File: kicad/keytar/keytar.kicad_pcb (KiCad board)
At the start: 2 copper layers, 70 x 90 mm, 40 parts, among them J1 , J2 USB_B, J3 AudioJack2, J4 Conn_01x04, J5 USB_A, J6 Mini-DIN-6-Shielded, J7 Conn_01x04, Q1 BSS138, Q2 BSS138, SW1 SW_DPST_x2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

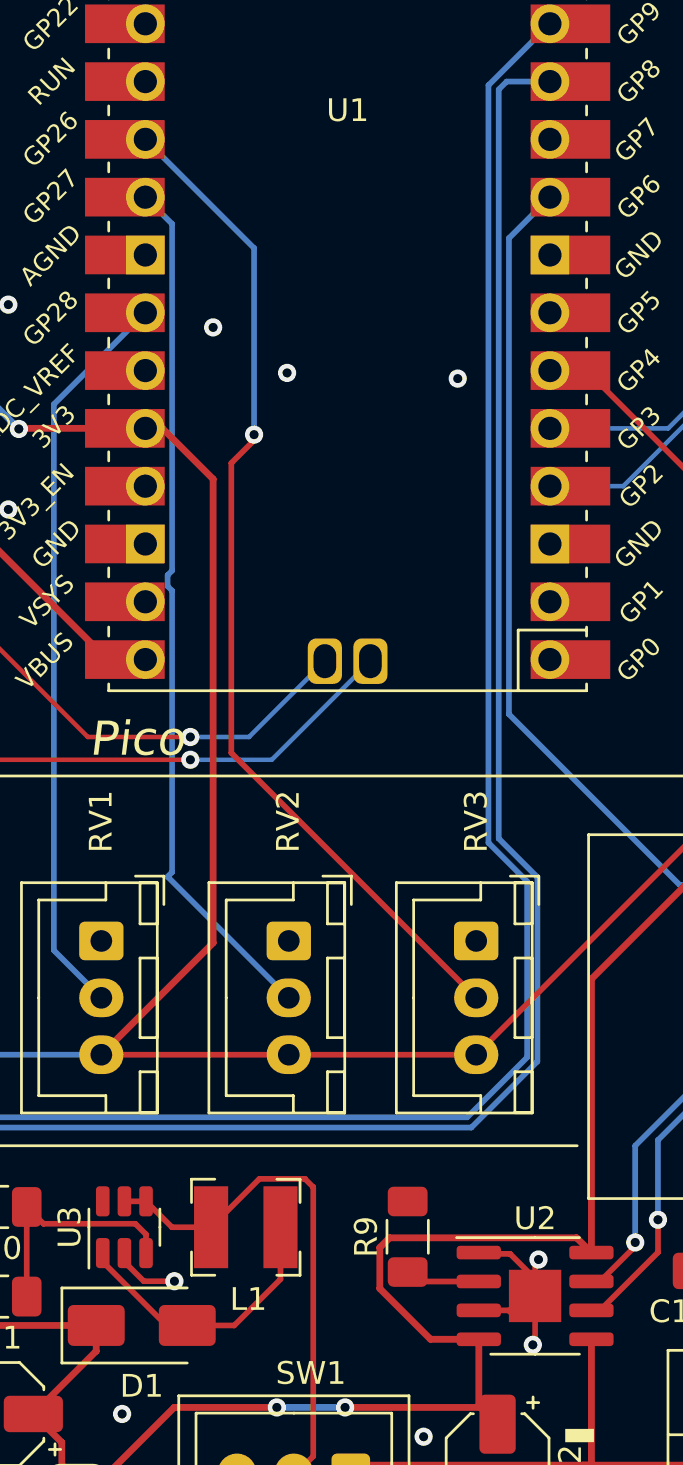
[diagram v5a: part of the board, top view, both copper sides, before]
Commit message: kicad: add voltage divider for battery voltage measurement
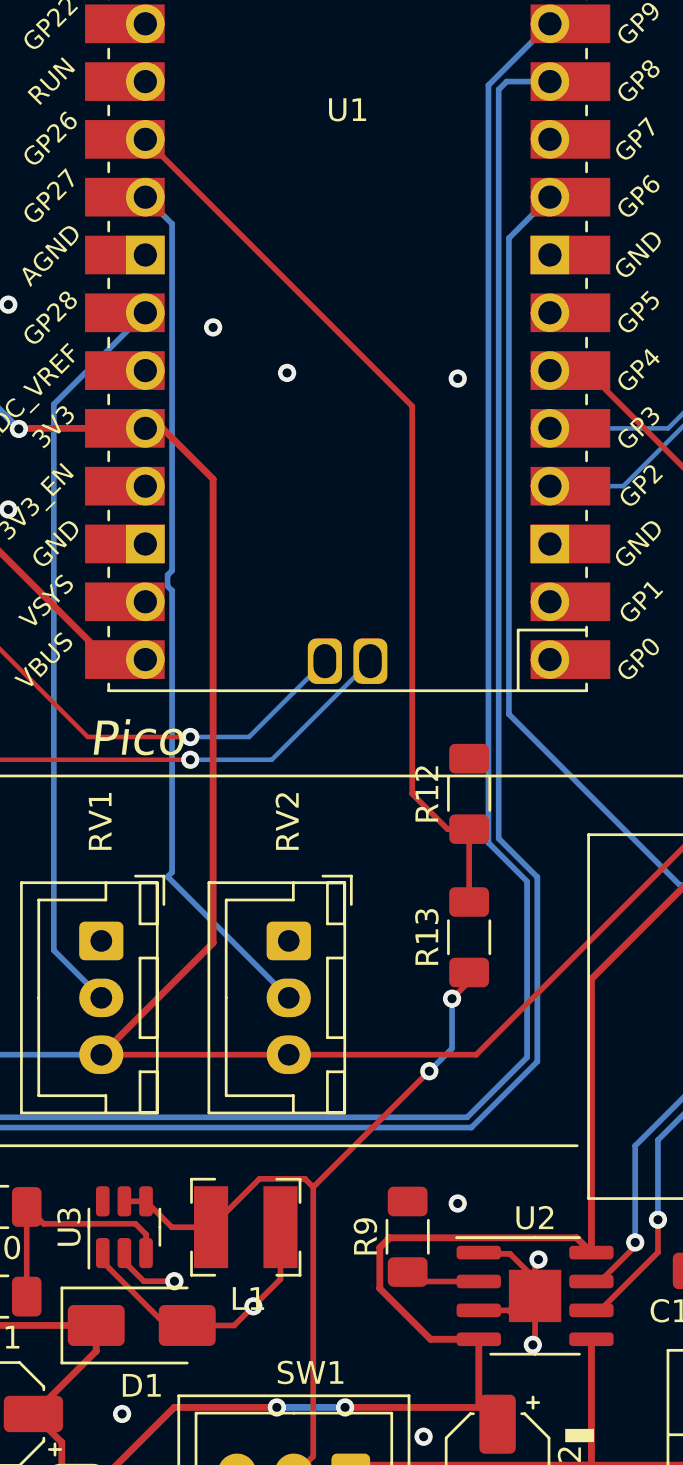
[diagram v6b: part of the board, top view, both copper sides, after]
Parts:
- removed RV3: R_POT, Connector_JST:JST_XH_B3B-XH-A_1x03_P2.50mm_Vertical
- added R12: 100k, Resistor_SMD:R_1206_3216Metric_Pad1.30x1.75mm_HandSolder, F.Cu at (140.2, 107.0)
- added R13: 100k, Resistor_SMD:R_1206_3216Metric_Pad1.30x1.75mm_HandSolder, F.Cu at (140.2, 113.3)
- J1: value (none) -> ~
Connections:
- net /REG_IN renamed BATT MEASURE
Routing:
- net BATT MEASURE: track 22.8 -> 35.1 mm, vias 0 -> 2
- net Net-(U1-GPIO26_ADC0): track 44.6 -> 40.0 mm, vias 1 -> 0
- net /REG_OUT: vias 0 -> 1
- net GND: vias 14 -> 15
